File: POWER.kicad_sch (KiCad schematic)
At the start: 16 parts, among them U6 TPS7A2033PDQNR, U7 TPSM82822SILR, U8 TPSM82822SILR

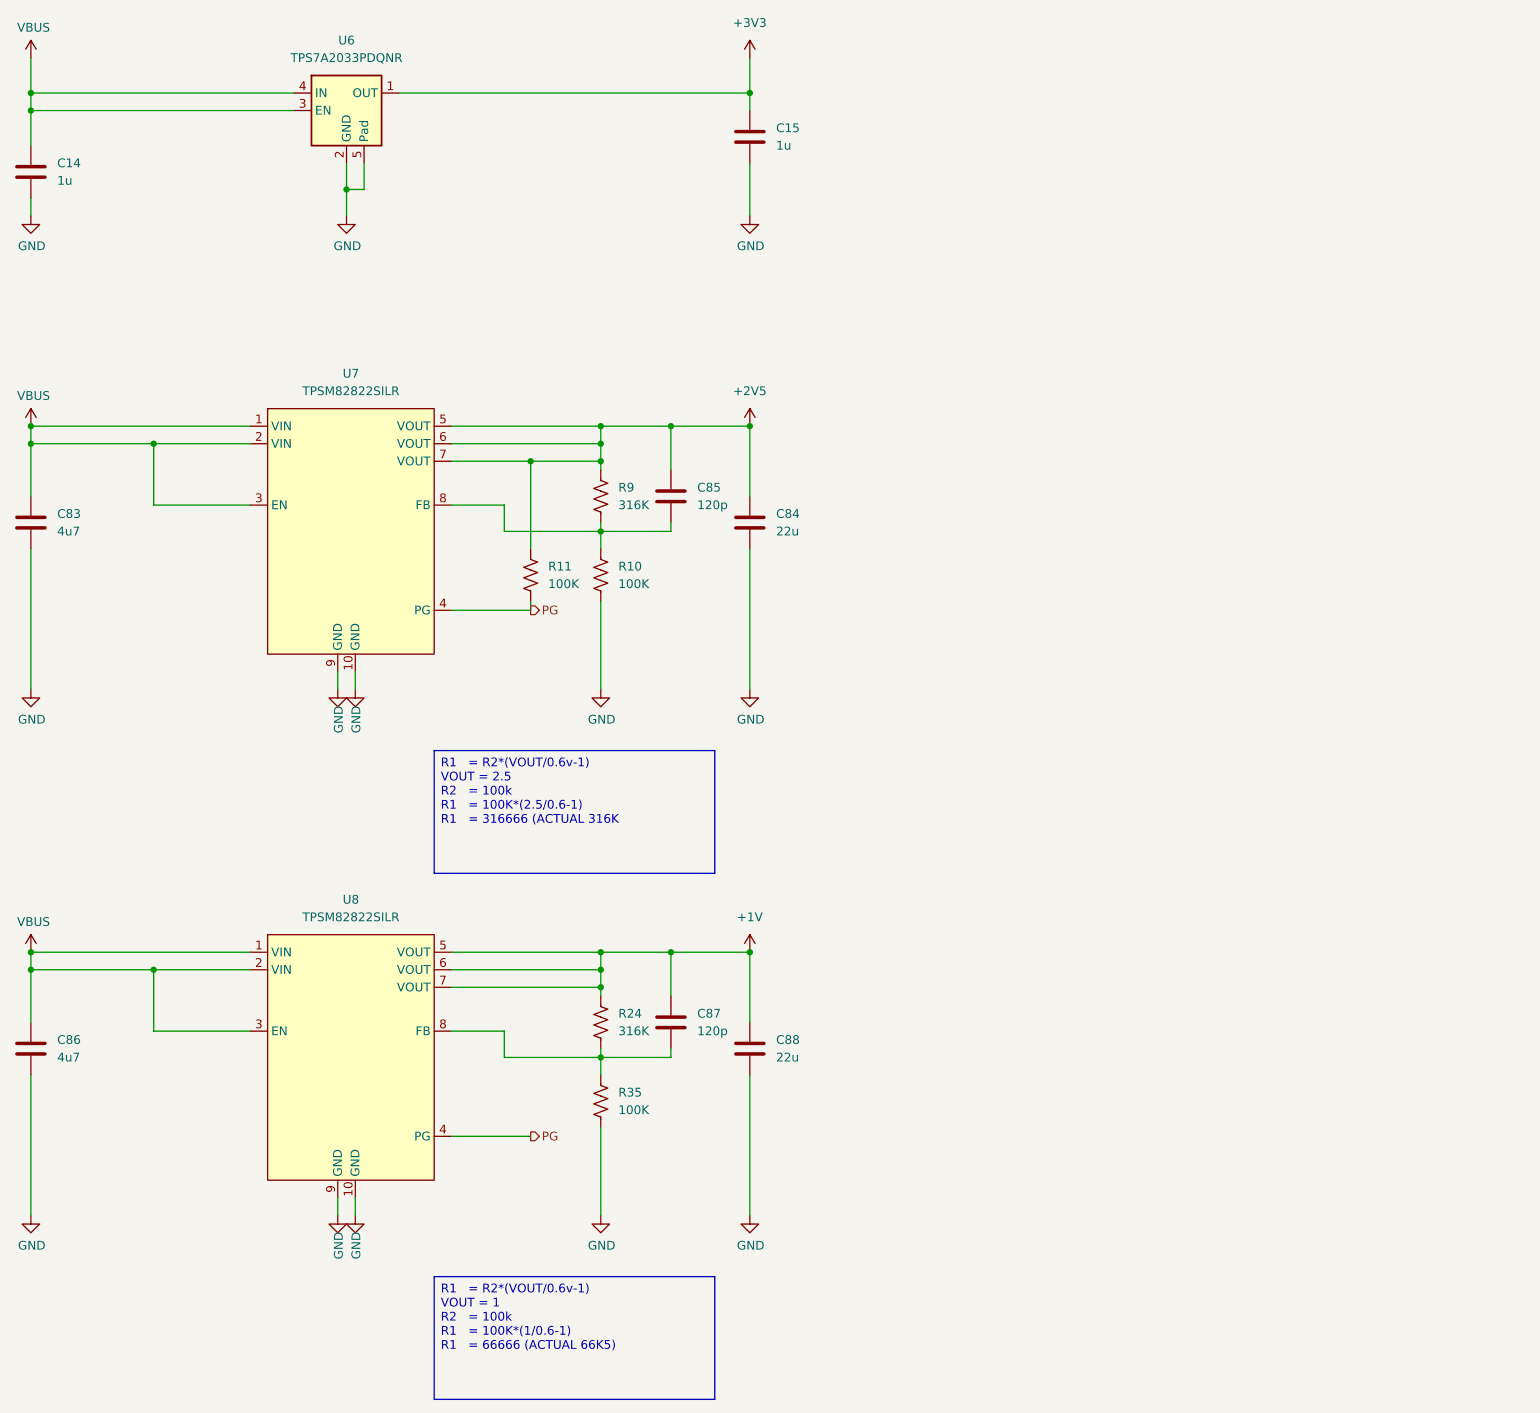
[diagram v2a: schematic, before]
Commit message: update on layout first drc done
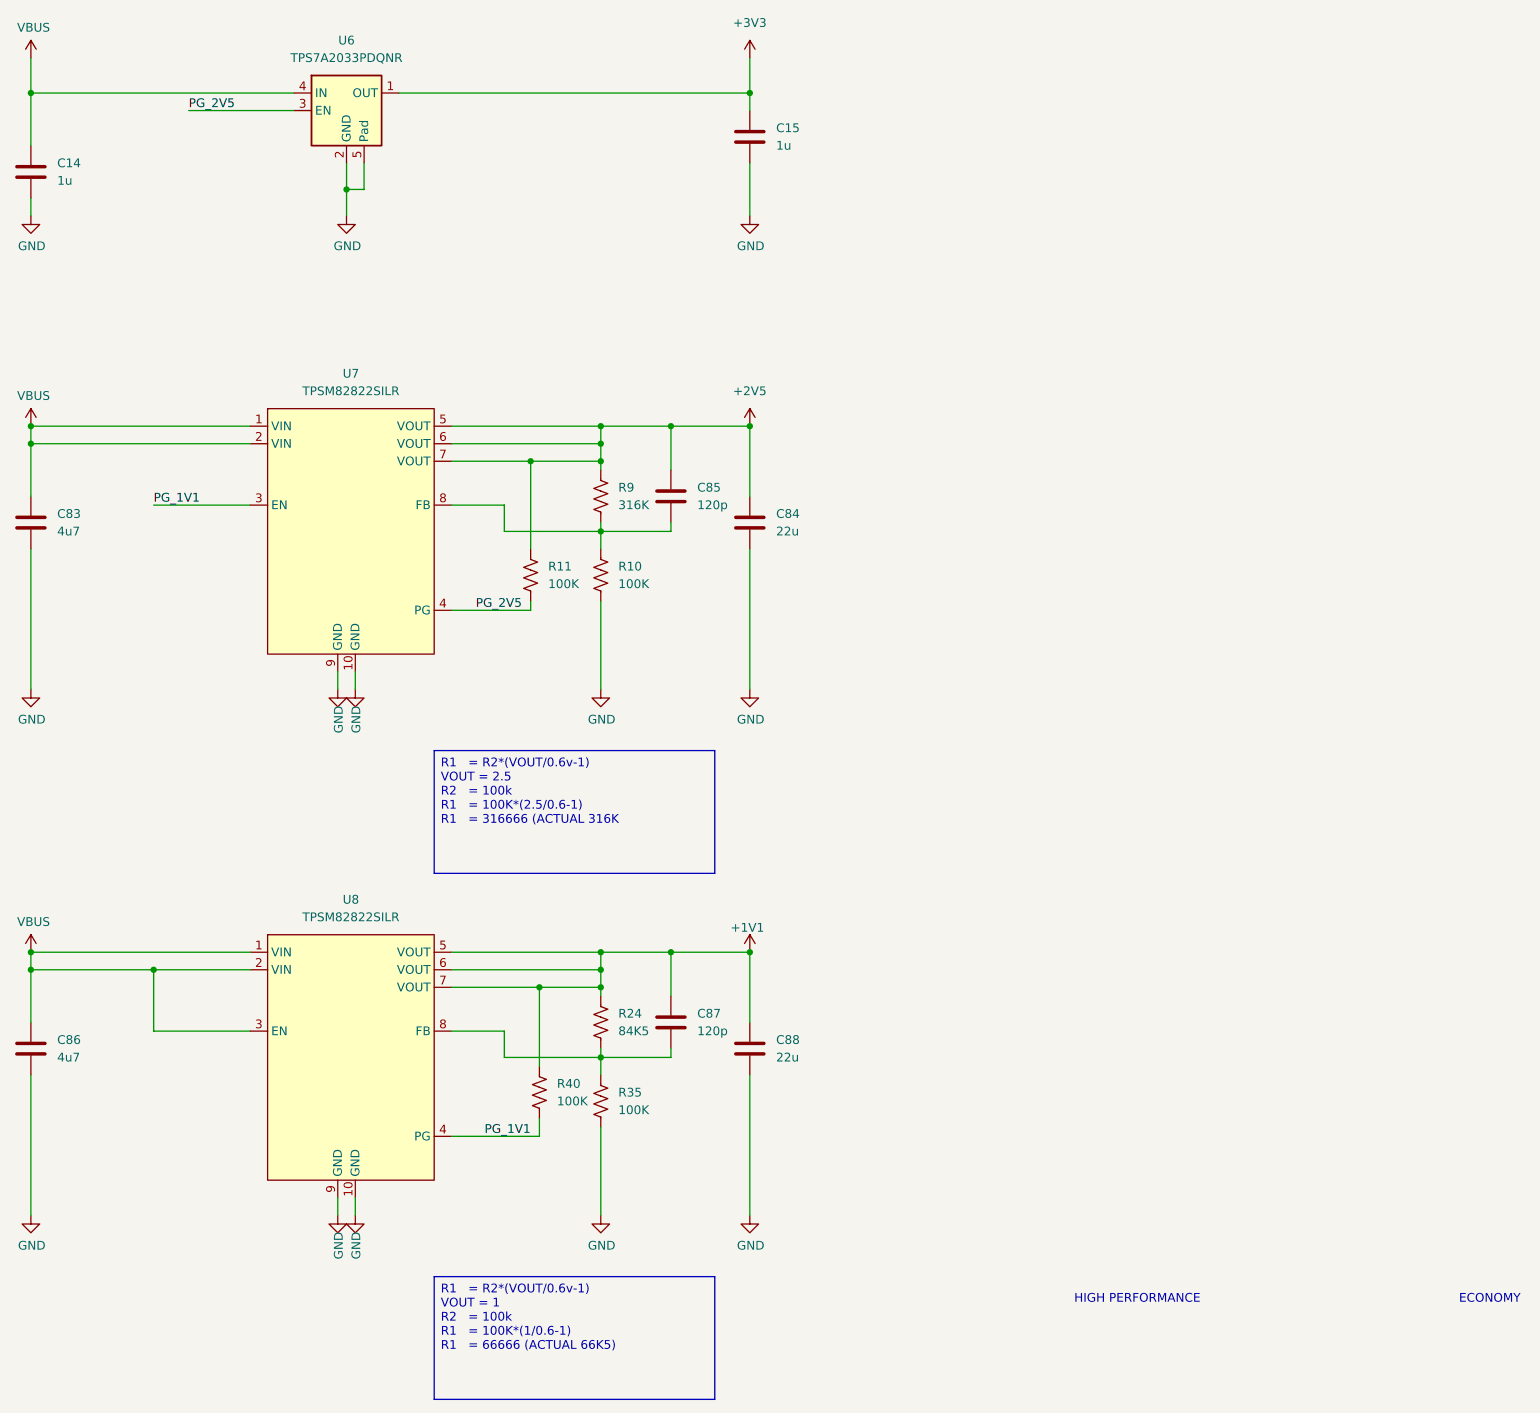
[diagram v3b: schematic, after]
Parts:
- added R40: 100K, Resistor_SMD:R_0201_0603Metric, symbol Device:R_US
- R24: value 316K -> 84K5
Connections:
- net VBUS: no longer U6.3 (EN), U7.3 (EN)
- net +1V renamed +1V1
- net +1V1: now also R40.1
- net PG renamed PG_2V5
- net PG_2V5: now also U6.3 (EN); no longer U8.4 (PG)
- new net PG_1V1: R40.2, U7.3 (EN), U8.4 (PG)
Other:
- note added: "ECONOMY"
- note added: "HIGH PERFORMANCE"

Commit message: RevA
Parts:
- C100: renamed from C15; MPN (none) -> CL05A105KA5NQNC
- C101: renamed from C14; MPN (none) -> CL05A105KA5NQNC
- C102: renamed from C85; MPN (none) -> GRM033R71E121KA01D
- C105: renamed from C87; MPN (none) -> GRM033R71E121KA01D
- R48: renamed from R9; MPN (none) -> RC0201FR-07316KL
- R49: renamed from R11; MPN (none) -> RC0201FR-07100KL
- R50: renamed from R10; MPN (none) -> RC0201FR-07100KL
- R51: renamed from R24; MPN (none) -> RC0201FR-0784K5L
- R52: renamed from R40; MPN (none) -> RC0201FR-07100KL
- R53: renamed from R35; MPN (none) -> RC0201FR-07100KL
- renumbered C83 to C103, C84 to C104, C86 to C106, C88 to C107, U7 to U10, U8 to U11, U6 to U9
